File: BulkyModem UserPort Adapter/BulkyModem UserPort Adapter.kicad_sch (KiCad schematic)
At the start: 9 parts, among them J1 C64_UserPort, J3 BulkyModem, M1 Mounting, M2 Mounting, M3 Mounting, M4 Mounting, U1 74HCT244

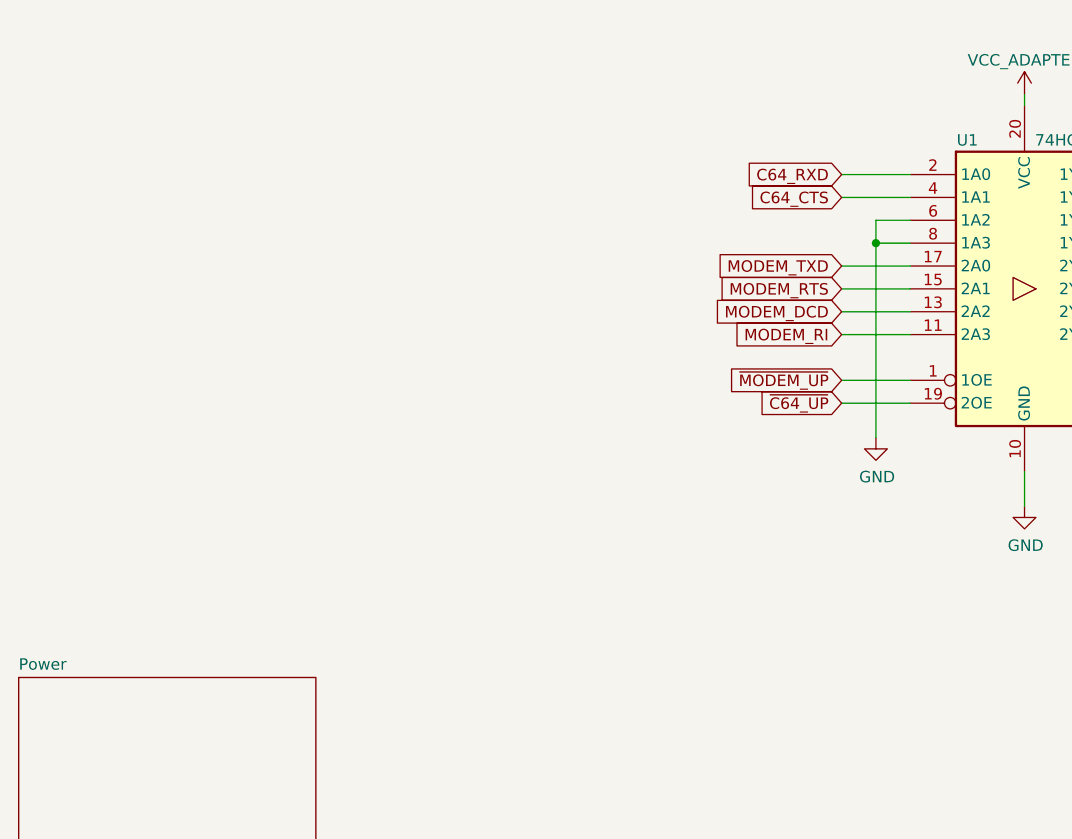
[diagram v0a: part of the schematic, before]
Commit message: Change UserPort transmitter to only enable on both parties present
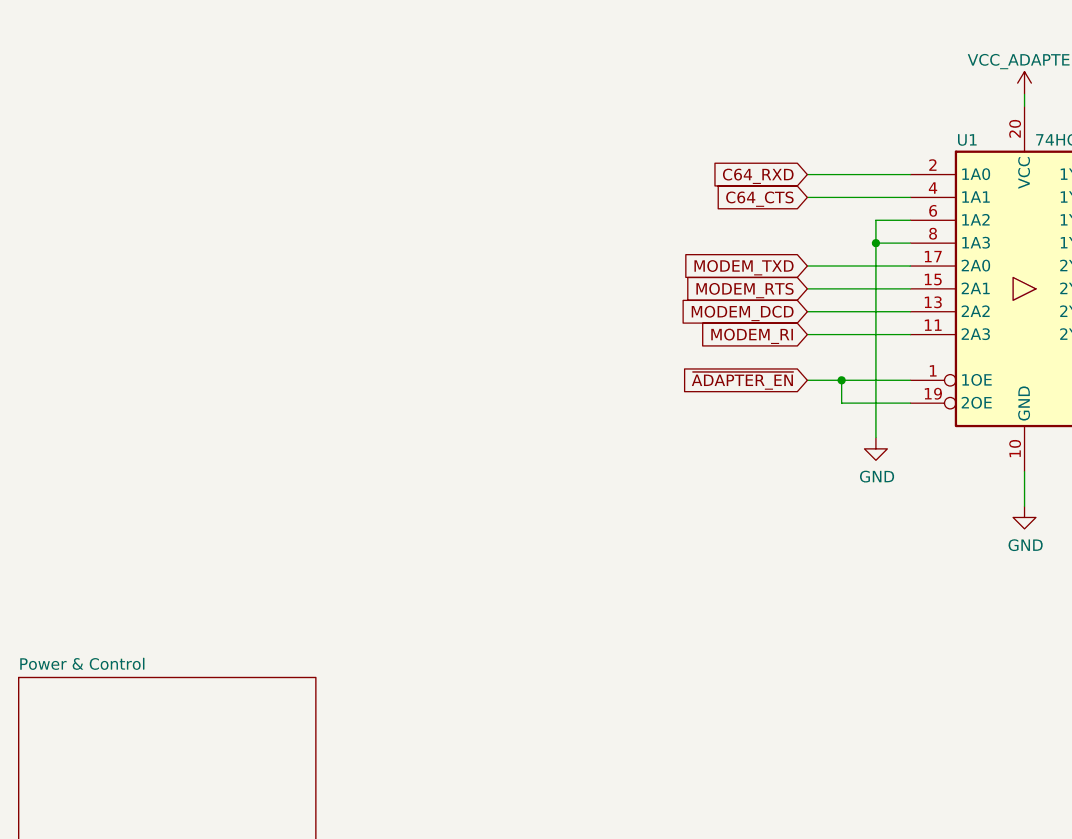
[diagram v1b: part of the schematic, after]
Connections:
- net ~{MODEM_UP} is gone; now on net ~{ADAPTER_EN}: U1.1 (1OE)
- net ~{C64_UP} renamed ~{ADAPTER_EN}
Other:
- sheet Power renamed Power & Control
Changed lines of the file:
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@@
 	(title_block
 		(title "BulkyModem (C64 UserPort Adapter)")
+		(rev "C")
 		(comment 4 "UserPort adapter for connecting to the BulkyModem via a 2x8-pin IDC cable.")
 	)
@@
 	)
 	(junction
+		(at 129.54 129.54)
+		(diameter 0)
+		(color 0 0 0 0)
+	)
+	(junction
 		(at 278.13 21.59)
 		(diameter 0)
@@
 	(wire
 		(pts
+			(xy 125.73 106.68) (xy 137.16 106.68)
+		)
+		(stroke
+			(width 0)
+			(type default)
+		)
+	)
+	(wire
+		(pts
 			(xy 63.5 44.45) (xy 60.96 44.45)
 		)
@@
 	(wire
 		(pts
+			(xy 125.73 121.92) (xy 137.16 121.92)
+		)
+		(stroke
+			(width 0)
+			(type default)
+		)
+	)
+	(wire
+		(pts
 			(xy 67.31 52.07) (xy 60.96 52.07)
 		)
@@
 	(wire
 		(pts
-			(xy 129.54 119.38) (xy 137.16 119.38)
-		)
-		(stroke
-			(width 0)
-			(type default)
-		)
-	)
-	(wire
-		(pts
 			(xy 237.49 53.34) (xy 241.3 53.34)
 		)
@@
 	(wire
 		(pts
+			(xy 125.73 124.46) (xy 137.16 124.46)
+		)
+		(stroke
+			(width 0)
+			(type default)
+		)
+	)
+	(wire
+		(pts
 			(xy 67.31 62.23) (xy 63.5 62.23)
 		)
@@
 	(wire
 		(pts
+			(xy 125.73 119.38) (xy 137.16 119.38)
+		)
+		(stroke
+			(width 0)
+			(type default)
+		)
+	)
+	(wire
+		(pts
 			(xy 63.5 44.45) (xy 67.31 44.45)
 		)
@@
 	(wire
 		(pts
-			(xy 129.54 124.46) (xy 137.16 124.46)
-		)
-		(stroke
-			(width 0)
-			(type default)
-		)
-	)
-	(wire
-		(pts
 			(xy 209.55 53.34) (xy 213.36 53.34)
 		)
@@
 	(wire
 		(pts
+			(xy 125.73 109.22) (xy 137.16 109.22)
+		)
+		(stroke
+			(width 0)
+			(type default)
+		)
+	)
+	(wire
+		(pts
 			(xy 241.3 48.26) (xy 241.3 50.8)
 		)
@@
 	(wire
 		(pts
+			(xy 125.73 129.54) (xy 129.54 129.54)
+		)
+		(stroke
+			(width 0)
+			(type default)
+		)
+	)
+	(wire
+		(pts
 			(xy 241.3 43.18) (xy 241.3 45.72)
 		)
@@
 	(wire
 		(pts
-			(xy 129.54 116.84) (xy 137.16 116.84)
-		)
-		(stroke
-			(width 0)
-			(type default)
-		)
-	)
-	(wire
-		(pts
 			(xy 241.3 55.88) (xy 241.3 59.69)
 		)
@@
 	(wire
 		(pts
-			(xy 129.54 121.92) (xy 137.16 121.92)
-		)
-		(stroke
-			(width 0)
-			(type default)
-		)
-	)
-	(wire
-		(pts
 			(xy 237.49 55.88) (xy 241.3 55.88)
 		)
@@
 	(wire
 		(pts
-			(xy 129.54 106.68) (xy 137.16 106.68)
-		)
-		(stroke
-			(width 0)
-			(type default)
-		)
-	)
-	(wire
-		(pts
 			(xy 237.49 45.72) (xy 241.3 45.72)
 		)
@@
 	(wire
 		(pts
-			(xy 129.54 109.22) (xy 137.16 109.22)
-		)
-		(stroke
-			(width 0)
-			(type default)
-		)
-	)
-	(wire
-		(pts
 			(xy 63.5 41.91) (xy 63.5 44.45)
 		)
@@
 	(wire
 		(pts
+			(xy 125.73 116.84) (xy 137.16 116.84)
+		)
+		(stroke
+			(width 0)
+			(type default)
+		)
+	)
+	(wire
+		(pts
 			(xy 100.33 67.31) (xy 107.95 67.31)
 		)
@@
 		(pts
 			(xy 278.13 21.59) (xy 281.94 21.59)
+		)
+		(stroke
+			(width 0)
+			(type default)
+		)
+	)
+	(wire
+		(pts
+			(xy 129.54 129.54) (xy 129.54 132.08)
 		)
 		(stroke
@@
 		)
 	)
-	(global_label "~{MODEM_UP}"
-		(shape input)
-		(at 129.54 129.54 180)
-		(fields_autoplaced yes)
-		(effects
-			(font
-				(size 1.27 1.27)
-			)
-			(justify right)
-		)
-		(property "Intersheetrefs" "${INTERSHEET_REFS}"
-			(at 116.9886 129.54 0)
-			(effects
-				(font
-					(size 1.27 1.27)
-				)
-				(justify right)
-				(hide yes)
-			)
-		)
-	)
 	(global_label "C64_RXD"
 		(shape input)
-		(at 129.54 106.68 180)
+		(at 125.73 106.68 180)
 		(effects
 			(font
@@
 		)
 		(property "Intersheetrefs" "${INTERSHEET_REFS}"
-			(at 129.54 106.68 0)
+			(at 125.73 106.68 0)
 			(effects
 				(font
@@
 	(global_label "MODEM_RI"
 		(shape input)
-		(at 129.54 124.46 180)
+		(at 125.73 124.46 180)
 		(effects
 			(font
@@
 		)
 		(property "Intersheetrefs" "${INTERSHEET_REFS}"
-			(at 129.54 124.46 0)
+			(at 125.73 124.46 0)
 			(effects
 				(font
@@
 		)
 	)
+	(global_label "~{ADAPTER_EN}"
+		(shape input)
+		(at 125.73 129.54 180)
+		(fields_autoplaced yes)
+		(effects
+			(font
+				(size 1.27 1.27)
+			)
+			(justify right)
+		)
+		(property "Intersheetrefs" "${INTERSHEET_REFS}"
+			(at 111.8481 129.54 0)
+			(effects
+				(font
+					(size 1.27 1.27)
+				)
+				(justify right)
+				(hide yes)
+			)
+		)
+	)
 	(global_label "MODEM_TXD"
 		(shape input)
-		(at 129.54 116.84 180)
+		(at 125.73 116.84 180)
 		(effects
 			(font
@@
 		)
 		(property "Intersheetrefs" "${INTERSHEET_REFS}"
-			(at 129.54 116.84 0)
+			(at 125.73 116.84 0)
 			(effects
 				(font
@@
 		)
 	)
-	(global_label "~{C64_UP}"
-		(shape input)
-		(at 129.54 132.08 180)
-		(fields_autoplaced yes)
-		(effects
-			(font
-				(size 1.27 1.27)
-			)
-			(justify right)
-		)
-		(property "Intersheetrefs" "${INTERSHEET_REFS}"
-			(at 119.9519 132.08 0)
-			(effects
-				(font
-					(size 1.27 1.27)
-				)
-				(justify right)
-				(hide yes)
-			)
-		)
-	)
 	(global_label "C64_RTS"
 		(shape output)
@@
 	(global_label "MODEM_RTS"
 		(shape input)
-		(at 129.54 119.38 180)
+		(at 125.73 119.38 180)
 		(effects
 			(font
@@
 		)
 		(property "Intersheetrefs" "${INTERSHEET_REFS}"
-			(at 129.54 119.38 0)
+			(at 125.73 119.38 0)
 			(effects
 				(font
@@
 	(global_label "C64_CTS"
 		(shape input)
-		(at 129.54 109.22 180)
+		(at 125.73 109.22 180)
 		(effects
 			(font
@@
 		)
 		(property "Intersheetrefs" "${INTERSHEET_REFS}"
-			(at 129.54 109.22 0)
+			(at 125.73 109.22 0)
 			(effects
 				(font
@@
 	(global_label "MODEM_DCD"
 		(shape input)
-		(at 129.54 121.92 180)
+		(at 125.73 121.92 180)
 		(effects
 			(font
@@
 		)
 		(property "Intersheetrefs" "${INTERSHEET_REFS}"
-			(at 129.54 121.92 0)
+			(at 125.73 121.92 0)
 			(effects
 				(font
@@
 			(color 0 0 0 0.0000)
 		)
-		(property "Sheetname" "Power"
+		(property "Sheetname" "Power & Control"
 			(at 38.1 161.8484 0)
 			(effects
